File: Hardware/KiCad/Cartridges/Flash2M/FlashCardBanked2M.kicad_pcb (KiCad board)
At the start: 4 copper layers, 47.9 x 47.9 mm, 10 parts, among them IC1 AS29CF160B-55TIN, IC2 74595D, IC3 74244DW, IC4 74HC1G04GW

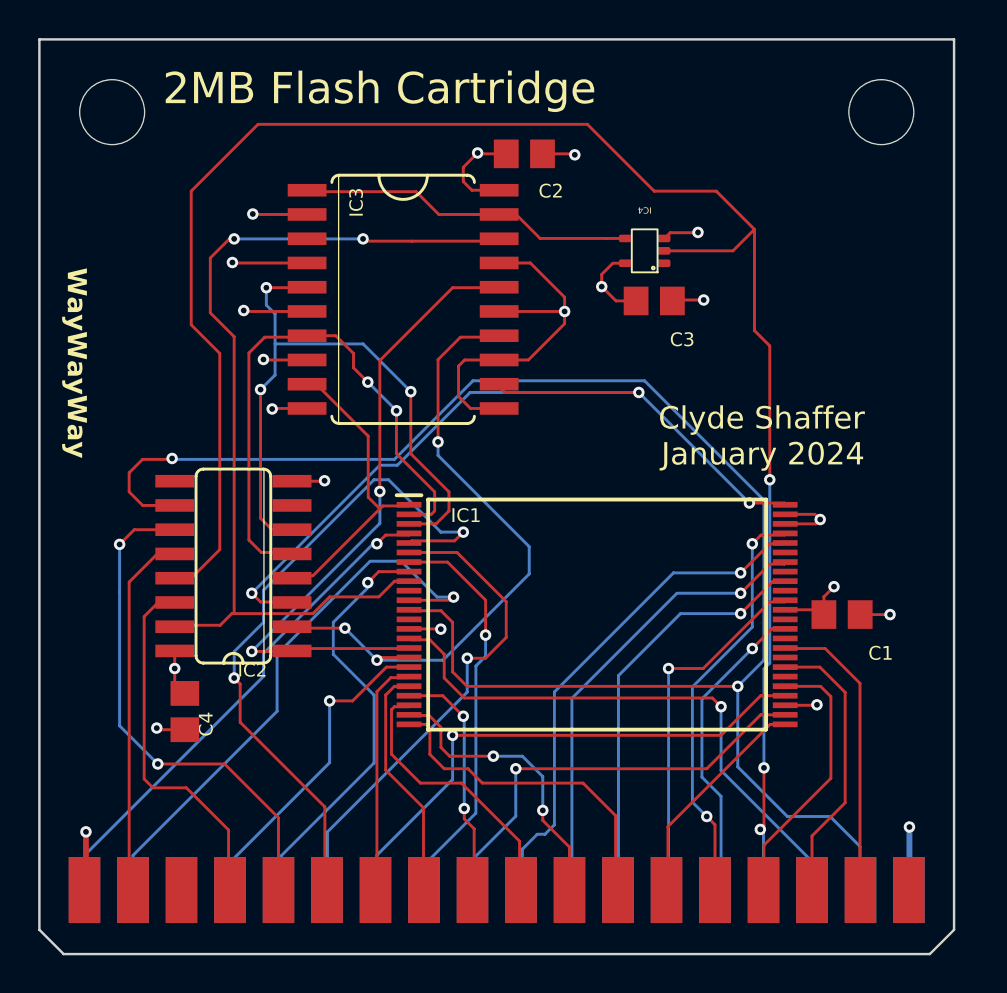
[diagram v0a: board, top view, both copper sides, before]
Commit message: add footprint for reset controller on logic board and remove READY on cartridges
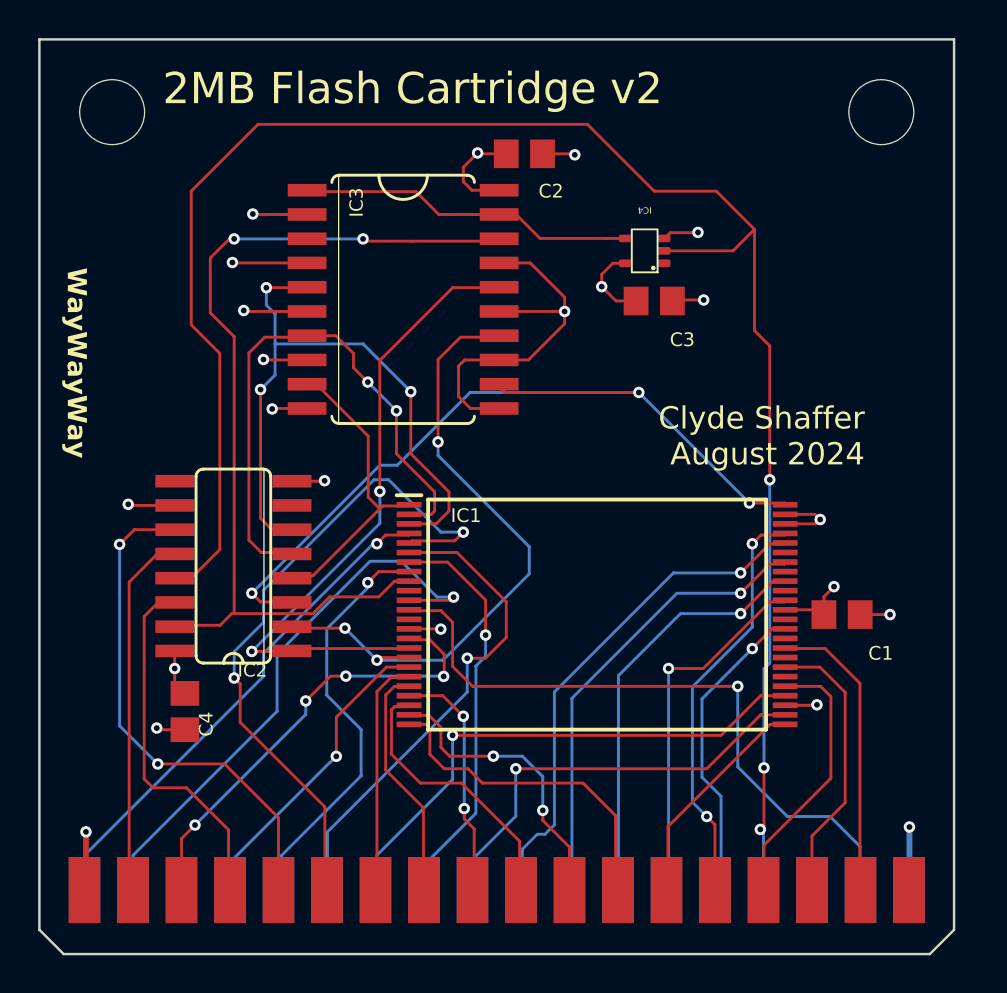
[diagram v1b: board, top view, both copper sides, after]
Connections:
- IC1 pad 15: /READY -> /FLASHBUSY
- IC2 pad 10: /~{RESET} -> VCC
- U$1 pad P$21: /READY -> unconnected-(U$1B-READY-PadP$21)
- U$1 pad P$3: unconnected-(U$1B-SPI_MISO-PadP$3) -> /FLASHBUSY
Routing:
- net /~{RESET}: track 86.9 -> 34.9 mm, vias 2 -> 1
- net /READY: track 30.2 -> 0.00 mm, vias 1 -> 0
- net /FLASHBUSY: track 0.00 -> 23.8 mm, vias 0 -> 4
- net VCC: track 52.5 -> 55.0 mm, vias 11 -> 12
- net /A7: track 17.0 -> 16.3 mm
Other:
- board text added: "2MB Flash Cartridge v2"
- board text added: "Clyde Shaffer August 2024"
- board text removed: "2MB Flash Cartridge"
- board text removed: "Clyde Shaffer January 2024"

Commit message: updates
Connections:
- IC2 pad 1: /A18 -> /A14
- IC2 pad 15: /A19 -> /A13
- IC2 pad 2: /A17 -> /A15
- IC2 pad 4: /A15 -> /A17
- IC2 pad 5: /A14 -> /A18
- IC2 pad 6: /A13 -> /A19
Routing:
- net /A17: track 33.7 -> 42.5 mm, vias 3 -> 2
- net /A13: track 34.2 -> 42.0 mm, vias 3 -> 4
- net /A14: track 29.8 -> 25.4 mm
- net /A18: track 34.2 -> 30.0 mm, vias 2 -> 4
- net /A19: track 48.1 -> 44.0 mm, vias 2 -> 4
- net /A15: track 16.2 -> 19.3 mm
- net /A16: track 44.6 -> 45.3 mm
- net /A11: track 35.5 -> 36.2 mm
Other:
- board text added: "2MB Flash Cartridge v2 MSB"
- board text added: "Clyde Shaffer December 2025"
- board text removed: "2MB Flash Cartridge v2"
- board text removed: "Clyde Shaffer August 2024"
